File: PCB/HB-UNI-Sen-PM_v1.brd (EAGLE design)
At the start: 40 x 40 mm, 27 parts, among them IC1 MCP1700T-3302E_MB, IC3 MEGA8-AI, Q1 CSTCE, U1 CC1101SMD

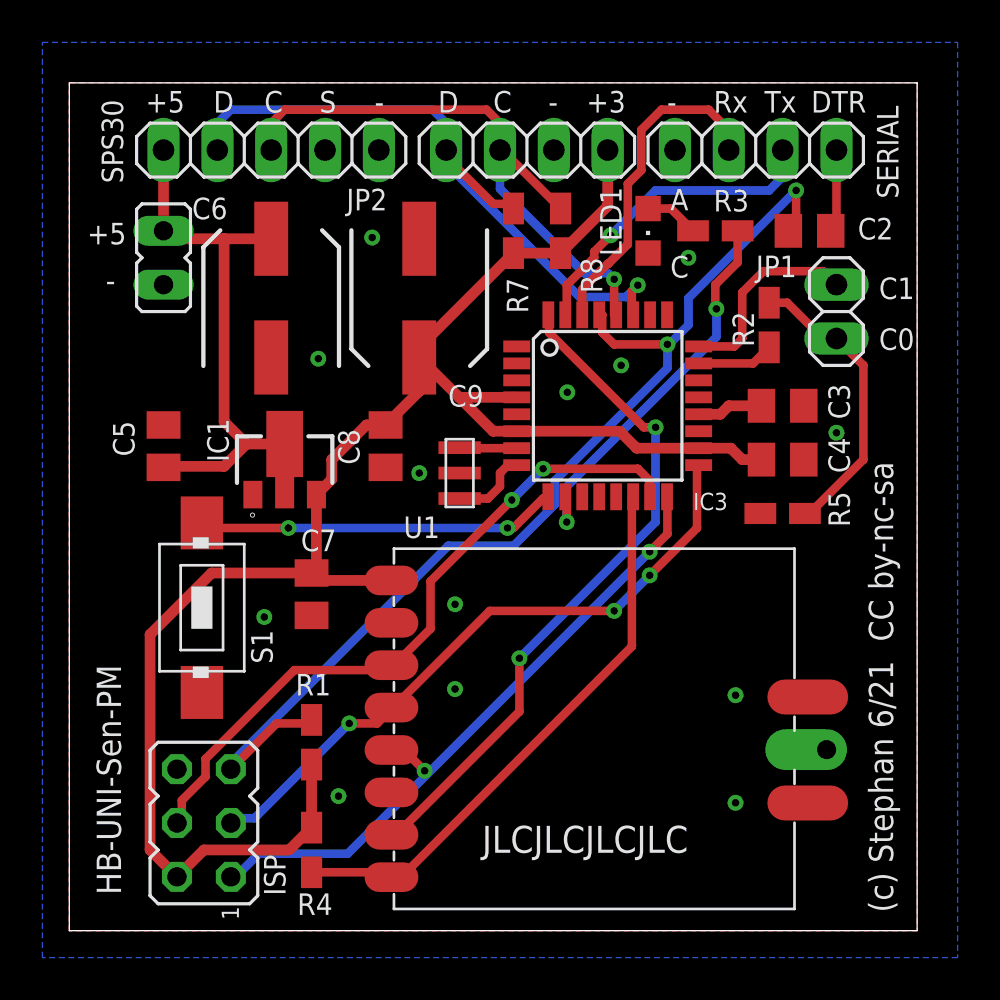
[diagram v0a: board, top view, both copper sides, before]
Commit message: pcb silkscreen corrected in v2.1, first working version of software
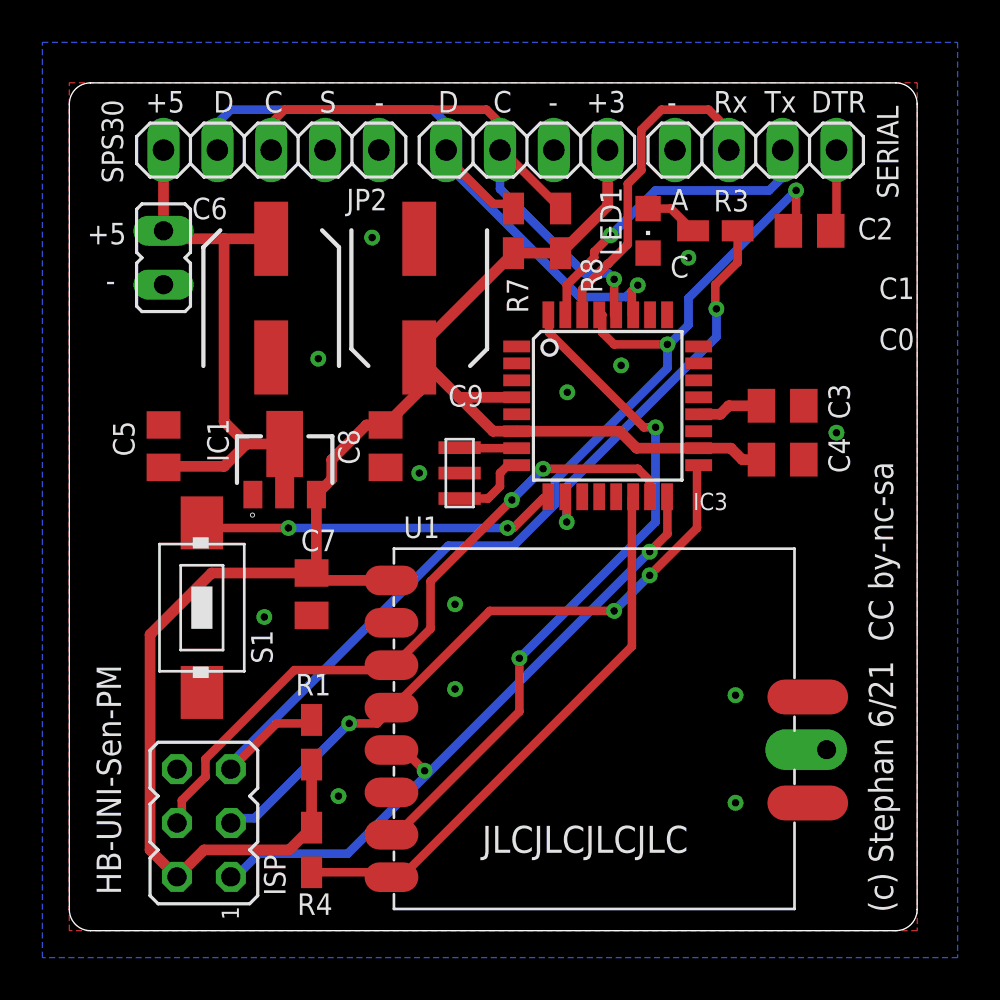
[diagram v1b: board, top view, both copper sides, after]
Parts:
- removed JP1: IO, pinhead:1X02
- removed R2, R5: 10k, resistor:R0805W
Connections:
- removed net PC0: IC3.23, R2.2
- removed net PC0DIV: JP1.1, R2.1, R5.2
- removed net PC1: IC3.24, JP1.2
- net GND: no longer R5.1
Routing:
- net PC0DIV: track 13.9 -> 0.00 mm
- net PC1: track 9.51 -> 0.00 mm
- net PC0: track 3.64 -> 0.00 mm
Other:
- outline, holes or cut-outs redrawn
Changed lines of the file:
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@@
 <grid distance="0.3175" unitdist="mm" unit="mm" style="lines" multiple="2" display="yes" altdistance="5" altunitdist="mil" altunit="mil"/>
 <layers>
-<layer number="1" name="Top" color="4" fill="1" visible="no" active="yes"/>
+<layer number="1" name="Top" color="4" fill="1" visible="yes" active="yes"/>
 <layer number="2" name="Route2" color="1" fill="3" visible="no" active="no"/>
 <layer number="3" name="Route3" color="4" fill="3" visible="no" active="no"/>
@@
 <layer number="14" name="Route14" color="1" fill="6" visible="no" active="no"/>
 <layer number="15" name="Route15" color="4" fill="6" visible="no" active="no"/>
-<layer number="16" name="Bottom" color="1" fill="1" visible="no" active="yes"/>
+<layer number="16" name="Bottom" color="1" fill="1" visible="yes" active="yes"/>
 <layer number="17" name="Pads" color="2" fill="1" visible="yes" active="yes"/>
 <layer number="18" name="Vias" color="2" fill="1" visible="yes" active="yes"/>
@@
 <board>
 <plain>
-<wire x1="0" y1="0" x2="40" y2="0" width="0" layer="20"/>
-<wire x1="40" y1="0" x2="40" y2="40" width="0" layer="20"/>
-<wire x1="40" y1="40" x2="0" y2="40" width="0" layer="20"/>
-<wire x1="0" y1="40" x2="0" y2="0" width="0" layer="20"/>
+<wire x1="0" y1="39" x2="0" y2="1" width="0" layer="20"/>
+<wire x1="0" y1="1" x2="1" y2="0" width="0" layer="20" curve="90"/>
+<wire x1="1" y1="0" x2="39" y2="0" width="0" layer="20"/>
+<wire x1="39" y1="0" x2="40" y2="1" width="0" layer="20" curve="90"/>
+<wire x1="40" y1="1" x2="40" y2="39" width="0" layer="20"/>
+<wire x1="40" y1="39" x2="39" y2="40" width="0" layer="20" curve="90"/>
+<wire x1="39" y1="40" x2="1" y2="40" width="0" layer="20"/>
+<wire x1="1" y1="40" x2="0" y2="39" width="0" layer="20" curve="90"/>
 <text x="3.6" y="38.6" size="1.016" layer="25">+5</text>
 <text x="2.69" y="33.3975" size="1.016" layer="25" rot="R180">+5</text>
@@
 <attribute name="VALUE" x="16.51" y="33.655" size="1.27" layer="27"/>
 </element>
-<element name="JP1" library="pinhead" library_urn="urn:adsk.eagle:library:325" package="1X02" package3d_urn="urn:adsk.eagle:package:22435/2" value="IO" x="36.195" y="29.21" smashed="yes" rot="R90">
-<attribute name="NAME" x="32.3938" y="30.8338" size="1.016" layer="25"/>
-<attribute name="VALUE" x="39.37" y="26.67" size="1.27" layer="27" rot="R90"/>
-</element>
-<element name="R2" library="resistor" library_urn="urn:adsk.eagle:library:348" package="R0805W" package3d_urn="urn:adsk.eagle:package:26060/1" value="10k" x="33.02" y="28.575" smashed="yes" rot="R270">
-<attribute name="NAME" x="31.29" y="29.21" size="1.016" layer="25" rot="R270"/>
-<attribute name="VALUE" x="30.48" y="29.21" size="1.27" layer="27" rot="R270"/>
-</element>
-<element name="R5" library="resistor" library_urn="urn:adsk.eagle:library:348" package="R0805W" package3d_urn="urn:adsk.eagle:package:26060/1" value="10k" x="33.655" y="19.685" smashed="yes">
-<attribute name="NAME" x="36.83" y="19.05" size="1.016" layer="25" rot="R90"/>
-<attribute name="VALUE" x="33.02" y="17.145" size="1.27" layer="27"/>
-</element>
 </elements>
 <signals>
@@
 <via x="23.495" y="25.4" extent="1-16" drill="0.35"/>
 <via x="36.195" y="23.495" extent="1-16" drill="0.35"/>
-<contactref element="R5" pad="1"/>
 <via x="18.2" y="15.4" extent="1-16" drill="0.35"/>
 <via x="18.2" y="11.4" extent="1-16" drill="0.35"/>
@@
 <wire x1="7.3025" y1="24.0175" x2="7.3025" y2="32.645" width="0.508" layer="1"/>
 </signal>
-<signal name="PC0DIV">
-<contactref element="R2" pad="1"/>
-<contactref element="R5" pad="2"/>
-<contactref element="JP1" pad="1"/>
-<wire x1="33.02" y1="29.6275" x2="33.8725" y2="29.6275" width="0.4064" layer="1"/>
-<wire x1="33.8725" y1="29.6275" x2="35.56" y2="27.94" width="0.4064" layer="1"/>
-<wire x1="35.56" y1="27.94" x2="36.195" y2="27.94" width="0.4064" layer="1"/>
-<wire x1="36.195" y1="27.94" x2="37.465" y2="26.67" width="0.4064" layer="1"/>
-<wire x1="37.465" y1="26.67" x2="37.465" y2="22.225" width="0.4064" layer="1"/>
-<wire x1="37.465" y1="22.225" x2="34.925" y2="19.685" width="0.4064" layer="1"/>
-<wire x1="34.925" y1="19.685" x2="34.7075" y2="19.685" width="0.4064" layer="1"/>
-</signal>
-<signal name="PC0">
-<contactref element="R2" pad="2"/>
-<contactref element="IC3" pad="23"/>
-<wire x1="29.6926" y1="26.765" x2="32.2625" y2="26.765" width="0.4064" layer="1"/>
-<wire x1="32.2625" y1="26.765" x2="33.02" y2="27.5225" width="0.4064" layer="1"/>
-</signal>
-<signal name="PC1">
-<contactref element="JP1" pad="2"/>
-<contactref element="IC3" pad="24"/>
-<wire x1="29.6926" y1="27.565" x2="31.375" y2="27.565" width="0.4064" layer="1"/>
-<wire x1="31.375" y1="27.565" x2="31.75" y2="27.94" width="0.4064" layer="1"/>
-<wire x1="31.75" y1="30.11039375" x2="32.75460625" y2="31.115" width="0.4064" layer="1"/>
-<wire x1="31.75" y1="27.94" x2="31.75" y2="30.11039375" width="0.4064" layer="1"/>
-<wire x1="35.56" y1="31.115" x2="36.195" y2="30.48" width="0.4064" layer="1"/>
-<wire x1="32.75460625" y1="31.115" x2="35.56" y2="31.115" width="0.4064" layer="1"/>
-</signal>
 </signals>
